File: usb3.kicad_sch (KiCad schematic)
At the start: 51 parts, among them J5 WE_632723300011_alt_symbol, Q4 NX138BKMYL, U17 HD3SS3220, U18 AP22615, U19 TPD4E05U06QDQARQ1, U20 TPD4E05U06QDQARQ1, U21 TPD4E05U06QDQARQ1

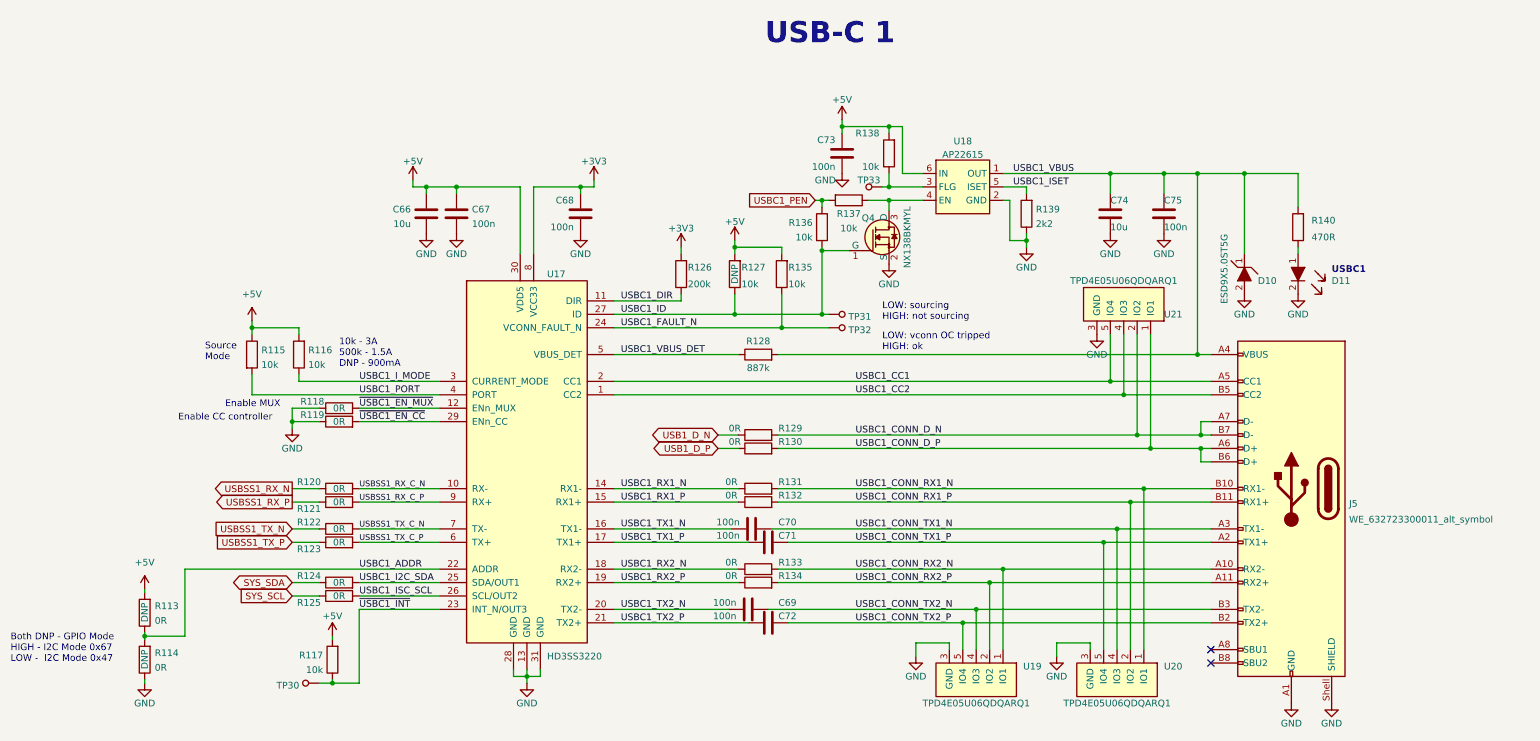
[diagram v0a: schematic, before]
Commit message: Aligned everything to 50mil grid
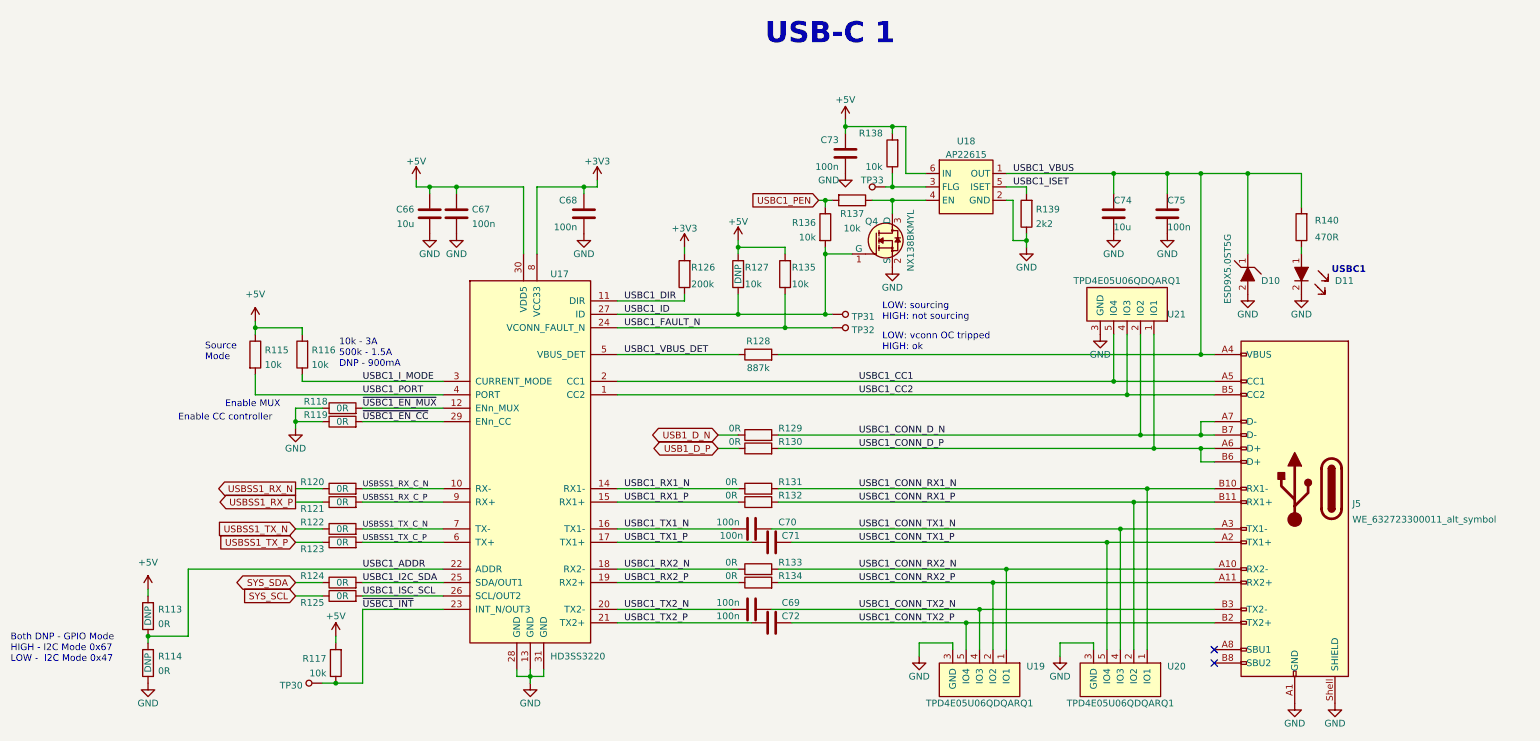
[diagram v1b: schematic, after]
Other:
- moved on the sheet: C66, C68, C69, C71, C72, C73, C74, C75, D10, D11, J5, Q4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

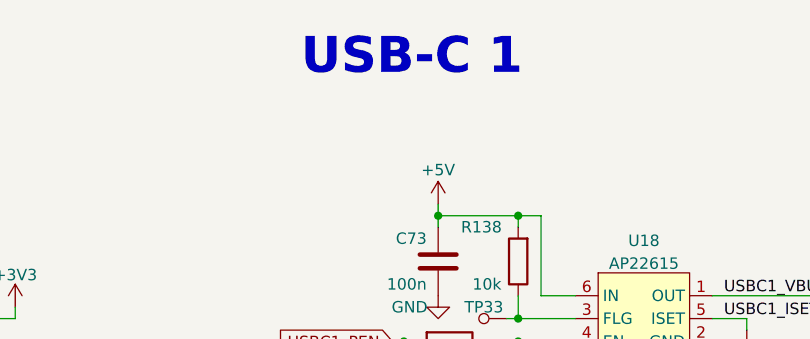
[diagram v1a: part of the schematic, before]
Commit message: Synchronized page fields and rearranged pages
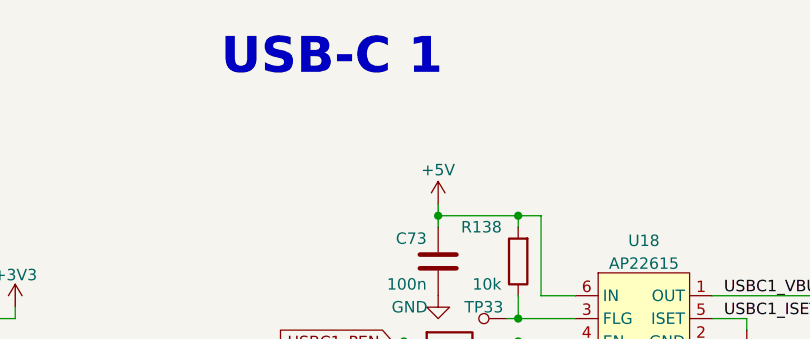
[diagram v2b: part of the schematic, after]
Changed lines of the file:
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@@
   (title_block
     (title "Jetson Orin Baseboard")
-    (date "2022-09-28")
+    (date "2022-10-07")
     (rev "1.0.0")
     (company "Antmicro Ltd")
@@
     (effects (font (size 1.27 1.27)) (justify left bottom))
   )
-  (text "USB-C 1" (at 204.47 71.12 0)
-    (effects (font (size 4 4) bold) (justify left bottom))
+  (text "USB-C 1" (at 195.58 71.12 0)
+    (effects (font (size 4 4) (thickness 0.8) bold) (justify left bottom))
   )
   (text "10k - 3A\n500k - 1.5A\nDNP - 900mA" (at 123.825 132.08 0)

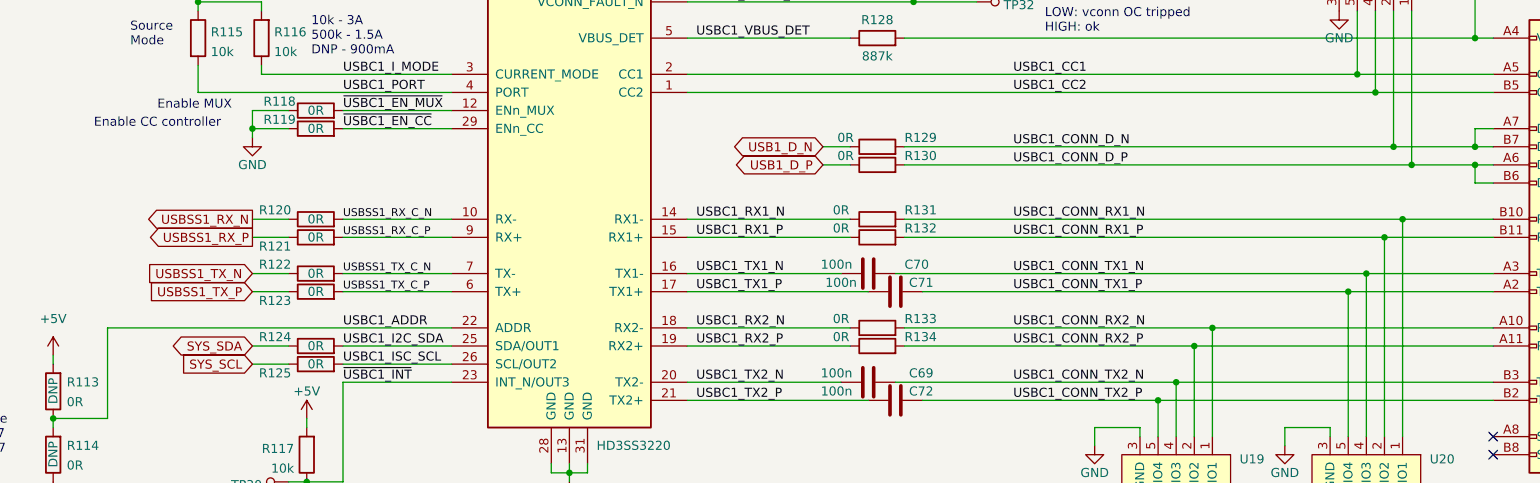
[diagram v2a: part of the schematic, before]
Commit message: Remove R0s from high speed signals, replace part of R0s with resistor ladder. Assign net clases
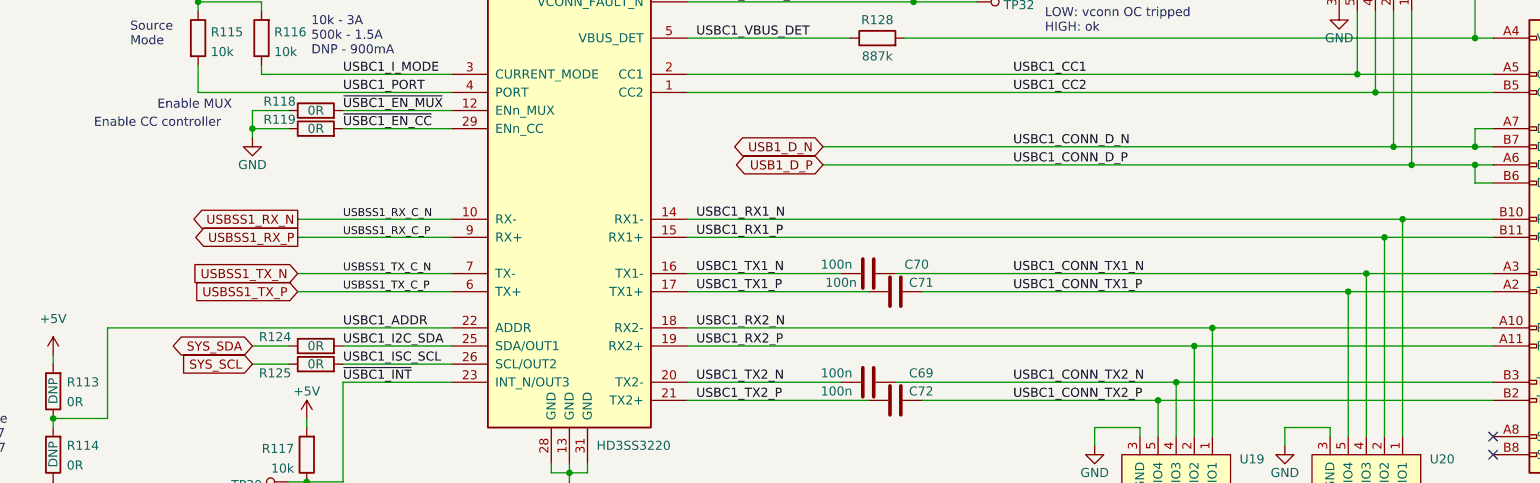
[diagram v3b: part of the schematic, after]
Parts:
- removed R120, R121, R122, R123, R129, R130, R131, R132, R133, R134: R_0R_0402, antmicro-footprints:0402-res, symbol antmicroResistors0402:R_0R_0402
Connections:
- net USBC1_CONN_D_N is gone; now on net USB1_D_N: J5.A7 (D-), J5.B7 (D-), U21.2 (IO2), U21.9 (IO2)
- net USBC1_CONN_D_P is gone; now on net USB1_D_P: J5.A6 (D+), J5.B6 (D+), U21.1 (IO1), U21.10 (IO1)
- net USBC1_CONN_RX1_N is gone; now on net USBC1_RX1_N: J5.B10 (RX1-), U20.1 (IO1), U20.10 (IO1)
- net USBC1_CONN_RX1_P is gone; now on net USBC1_RX1_P: J5.B11 (RX1+), U20.2 (IO2), U20.9 (IO2)
- net USBC1_CONN_RX2_N is gone; now on net USBC1_RX2_N: J5.A10 (RX2-), U19.1 (IO1), U19.10 (IO1)
- net USBC1_CONN_RX2_P is gone; now on net USBC1_RX2_P: J5.A11 (RX2+), U19.2 (IO2), U19.9 (IO2)
- net USBSS1_RX_C_N is gone; now on net USBSS1_RX_N: U17.10 (RX-)
- net USBSS1_RX_C_P is gone; now on net USBSS1_RX_P: U17.9 (RX+)
- net USBSS1_TX_C_N is gone; now on net USBSS1_TX_N: U17.7 (TX-)
- net USBSS1_TX_C_P is gone; now on net USBSS1_TX_P: U17.6 (TX+)

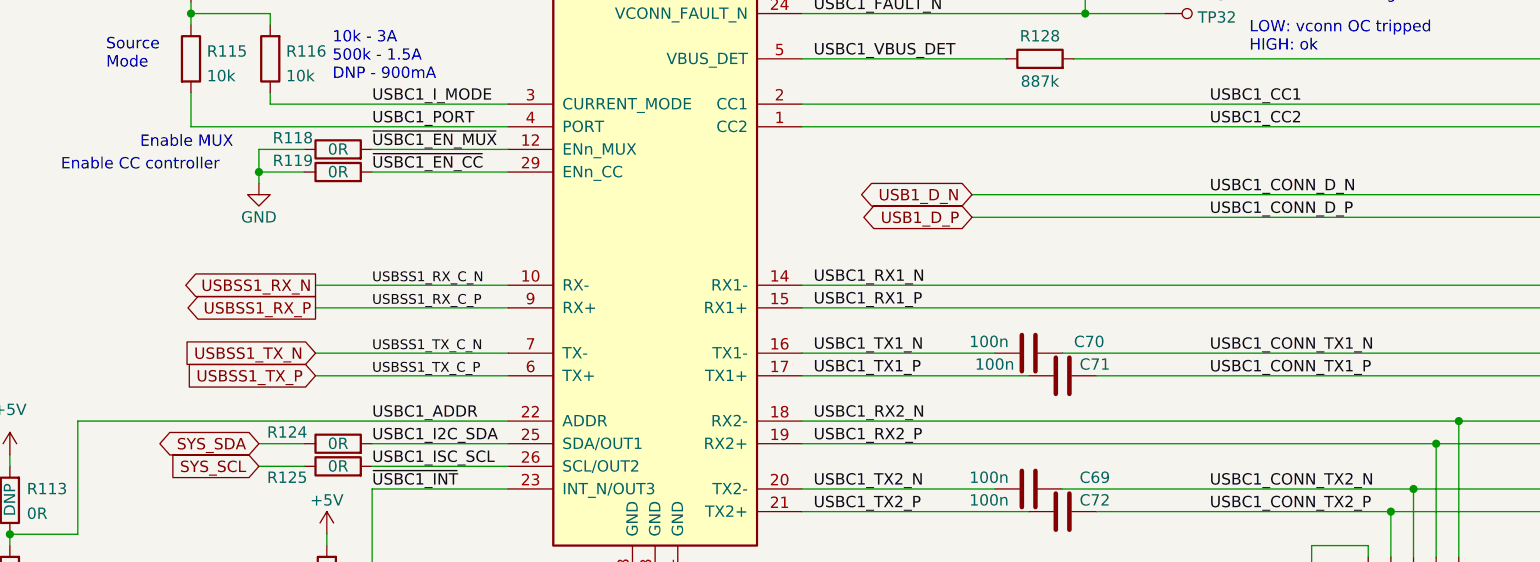
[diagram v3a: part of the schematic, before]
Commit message: Handled connection of unconnected pins and removed unnecessary labels
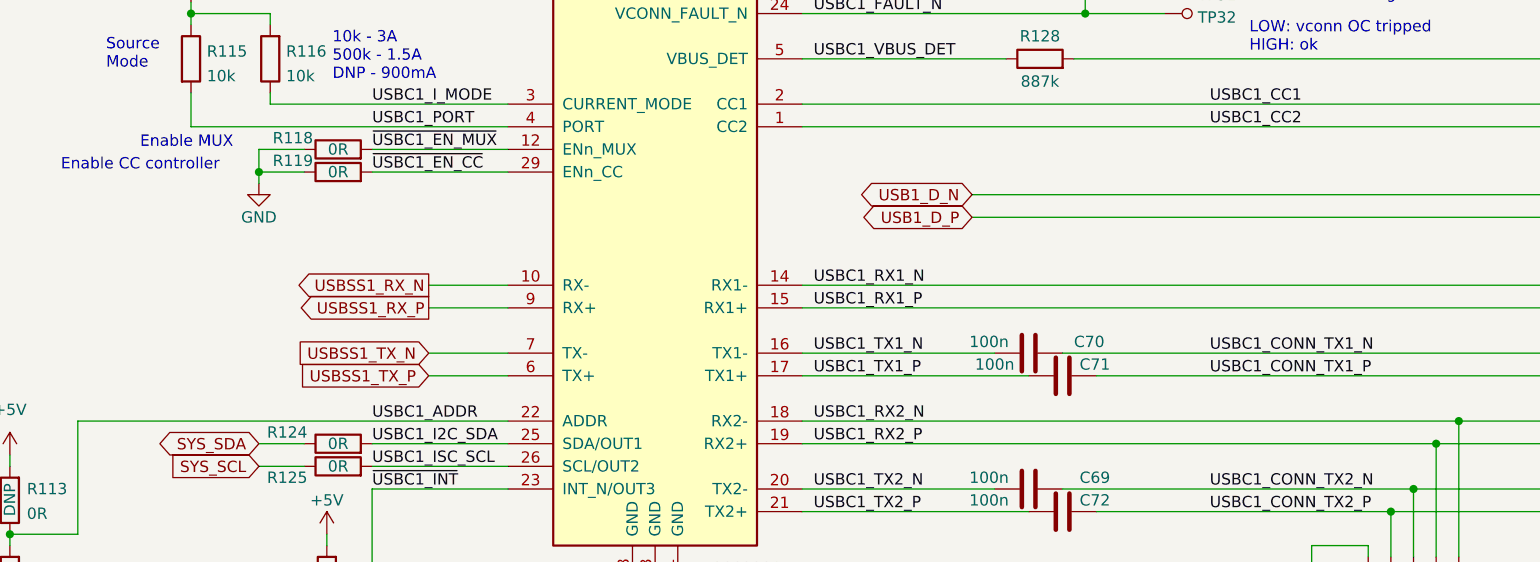
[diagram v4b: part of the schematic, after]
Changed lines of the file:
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@@
     (stroke (width 0) (type default) (color 0 0 0 0))
   )
-  (wire (pts (xy 121.92 162.56) (xy 143.51 162.56))
+  (wire (pts (xy 134.62 162.56) (xy 143.51 162.56))
     (stroke (width 0) (type default) (color 0 0 0 0))
   )
@@
     (stroke (width 0) (type default) (color 0 0 0 0))
   )
-  (wire (pts (xy 121.92 165.1) (xy 143.51 165.1))
+  (wire (pts (xy 134.62 165.1) (xy 143.51 165.1))
     (stroke (width 0) (type default) (color 0 0 0 0))
   )
@@
     (stroke (width 0) (type default) (color 0 0 0 0))
   )
-  (wire (pts (xy 121.92 154.94) (xy 143.51 154.94))
+  (wire (pts (xy 134.62 154.94) (xy 143.51 154.94))
     (stroke (width 0) (type default) (color 0 0 0 0))
   )
@@
     (stroke (width 0) (type default) (color 0 0 0 0))
   )
-  (wire (pts (xy 121.92 157.48) (xy 143.51 157.48))
+  (wire (pts (xy 134.62 157.48) (xy 143.51 157.48))
     (stroke (width 0) (type default) (color 0 0 0 0))
   )
@@
     (effects (font (size 1.27 1.27)) (justify left bottom))
   )
-  (label "USBSS1_TX_C_N" (at 128.27 162.56 0)
-    (effects (font (size 1.1 1.1)) (justify left bottom))
-  )
   (label "USBC1_ISC_SCL" (at 128.27 175.26 0)
     (effects (font (size 1.27 1.27)) (justify left bottom))
@@
     (effects (font (size 1.27 1.27)) (justify left bottom))
   )
-  (label "USBSS1_TX_C_P" (at 128.27 165.1 0)
-    (effects (font (size 1.1 1.1)) (justify left bottom))
-  )
   (label "USBC1_CONN_TX1_N" (at 222.25 162.56 0)
     (effects (font (size 1.27 1.27)) (justify left bottom))
@@
     (effects (font (size 1.27 1.27)) (justify left bottom))
   )
-  (label "USBSS1_RX_C_N" (at 128.27 154.94 0)
-    (effects (font (size 1.1 1.1)) (justify left bottom))
-  )
   (label "USBC1_CONN_TX1_P" (at 222.25 165.1 0)
     (effects (font (size 1.27 1.27)) (justify left bottom))
@@
     (effects (font (size 1.27 1.27)) (justify left bottom))
   )
-  (label "USBSS1_RX_C_P" (at 128.27 157.48 0)
-    (effects (font (size 1.1 1.1)) (justify left bottom))
-  )
   (label "USBC1_VBUS_DET" (at 177.8 129.54 0)
     (effects (font (size 1.27 1.27)) (justify left bottom))
@@
     (effects (font (size 1.27 1.27)) (justify left bottom))
   )
-  (label "USBC1_CONN_D_N" (at 222.25 144.78 0)
-    (effects (font (size 1.27 1.27)) (justify left bottom))
-  )
   (label "USBC1_I_MODE" (at 128.27 134.62 0)
     (effects (font (size 1.27 1.27)) (justify left bottom))
@@
   )
   (label "USBC1_RX2_P" (at 177.8 172.72 0)
-    (effects (font (size 1.27 1.27)) (justify left bottom))
-  )
-  (label "USBC1_CONN_D_P" (at 222.25 147.32 0)
     (effects (font (size 1.27 1.27)) (justify left bottom))
   )
@@
     )
   )
-  (global_label "USBSS1_RX_P" (shape output) (at 121.92 157.48 180)
+  (global_label "USBSS1_RX_P" (shape output) (at 134.62 157.48 180)
     (effects (font (size 1.27 1.27)) (justify right))
-    (property "Intersheet References" "${INTERSHEET_REFS}" (id 0) (at 105.41 157.48 0)
+    (property "Intersheet References" "${INTERSHEET_REFS}" (id 0) (at 118.11 157.48 0)
       (effects (font (size 1.1 1.1)) (justify right))
     )
@@
     )
   )
-  (global_label "USBSS1_RX_N" (shape output) (at 121.92 154.94 180)
+  (global_label "USBSS1_RX_N" (shape output) (at 134.62 154.94 180)
     (effects (font (size 1.27 1.27)) (justify right))
-    (property "Intersheet References" "${INTERSHEET_REFS}" (id 0) (at 105.41 154.94 0)
+    (property "Intersheet References" "${INTERSHEET_REFS}" (id 0) (at 118.11 154.94 0)
       (effects (font (size 1.1 1.1)) (justify right))
     )
   )
-  (global_label "USBSS1_TX_P" (shape input) (at 121.92 165.1 180)
+  (global_label "USBSS1_TX_P" (shape input) (at 134.62 165.1 180)
     (effects (font (size 1.27 1.27)) (justify right))
-    (property "Intersheet References" "${INTERSHEET_REFS}" (id 0) (at 105.41 165.1 0)
+    (property "Intersheet References" "${INTERSHEET_REFS}" (id 0) (at 118.11 165.1 0)
       (effects (font (size 1.1 1.1)) (justify right))
     )
   )
-  (global_label "USBSS1_TX_N" (shape input) (at 121.92 162.56 180)
+  (global_label "USBSS1_TX_N" (shape input) (at 134.62 162.56 180)
     (effects (font (size 1.27 1.27)) (justify right))
-    (property "Intersheet References" "${INTERSHEET_REFS}" (id 0) (at 105.41 162.56 0)
+    (property "Intersheet References" "${INTERSHEET_REFS}" (id 0) (at 118.11 162.56 0)
       (effects (font (size 1.1 1.1)) (justify right))
     )

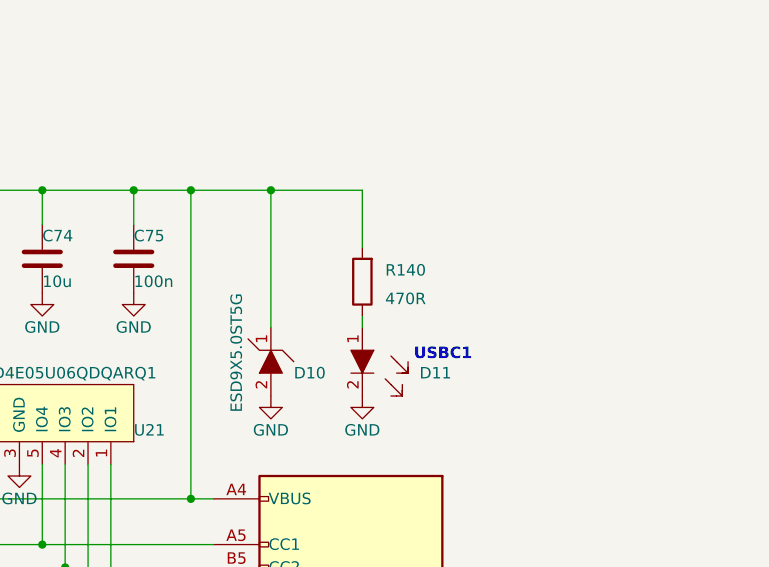
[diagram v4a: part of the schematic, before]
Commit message: Rearanged PCB to move M.2 connector and changed exp conn resistors to res arrays
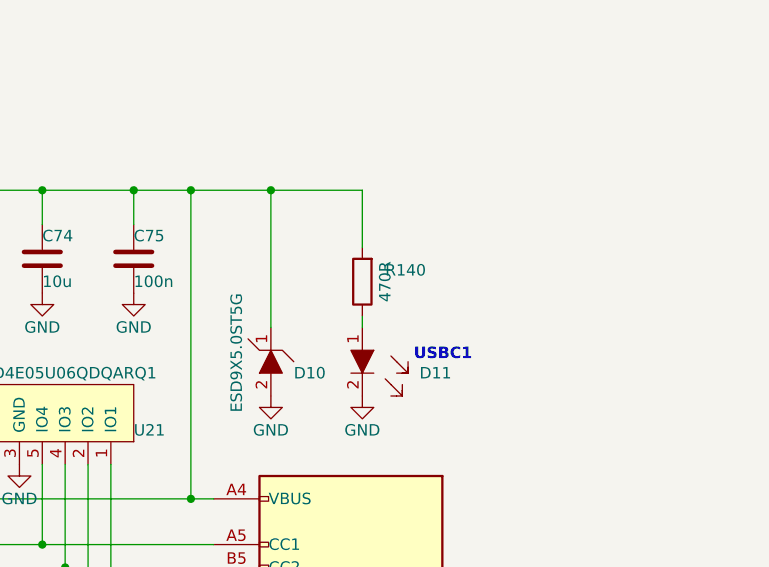
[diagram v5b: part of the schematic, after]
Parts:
- R140: value R_470R_0603 -> R_470R_0402; footprint antmicro-footprints:0603-res -> antmicro-footprints:0402-res; symbol antmicroResistors0603:R_470R_0603 -> antmicroResistors0402:R_470R_0402; MPN CR0603-JW-471GLF -> CRCW0402470RFKED; Manufacturer BOURNS -> VISHAY
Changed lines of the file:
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@@
     (pin "9")
   )
-  (symbol (lib_id "antmicroResistors0603:R_470R_0603") (at 306.07 105.41 90) (unit 1)
+  (symbol (lib_id "antmicroResistors0402:R_470R_0402") (at 306.07 105.41 90) (unit 1)
     (in_bom yes) (on_board yes) (fields_autoplaced)
     (property "Reference" "R140" (id 0) (at 308.61 104.14 90)
       (effects (font (size 1.27 1.27)) (justify right))
     )
-    (property "Value" "R_470R_0603" (id 1) (at 309.88 105.41 0)
-      (effects (font (size 1.27 1.27)) hide)
+    (property "Value" "R_470R_0402" (id 1) (at 309.88 105.41 0)
+      (effects (font (size 1.524 1.524)) hide)
     )
-    (property "Footprint" "antmicro-footprints:0603-res" (id 2) (at 300.99 100.33 0)
+    (property "Footprint" "antmicro-footprints:0402-res" (id 2) (at 300.99 100.33 0)
       (effects (font (size 1.524 1.524)) (justify left) hide)
     )
@@
       (effects (font (size 1.27 1.27)) hide)
     )
-    (property "Manufacturer" "BOURNS" (id 4) (at 295.91 100.33 0)
+    (property "Manufacturer" "VISHAY" (id 4) (at 295.91 100.33 0)
       (effects (font (size 1.524 1.524)) (justify left) hide)
     )
-    (property "MPN" "CR0603-JW-471GLF" (id 5) (at 298.45 100.33 0)
+    (property "MPN" "CRCW0402470RFKED" (id 5) (at 298.45 100.33 0)
       (effects (font (size 1.524 1.524)) (justify left) hide)
     )
-    (property "Val" "470R" (id 6) (at 308.61 107.3149 90)
-      (effects (font (size 1.27 1.27)) (justify right))
-    )
+    (property "Val" "470R" (id 6) (at 308.61 105.41 0))
     (pin "1")
     (pin "2")
